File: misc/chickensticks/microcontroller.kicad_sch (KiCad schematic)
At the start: 41 parts, among them J1 Conn_01x05_Pin, J2 HRO_TYPE-C-31-M-12, J3 Conn_01x04, J4 Conn_01x06, J5 Conn_01x06, J6 Conn_01x04, J7 Conn_01x04, Q3 2N7002, SW1 SKRPANE010, SW2 EC11E18244AU, U1 USBLC6-2SC6, U2 STM32L433CCTx, U3 TJA1042T-3, Y1 25 MHz

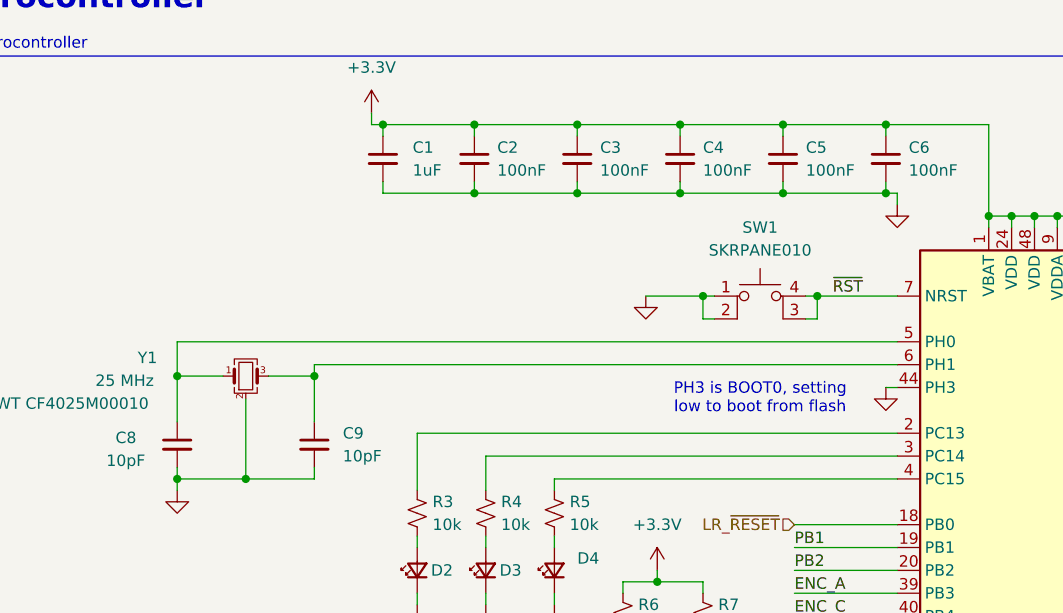
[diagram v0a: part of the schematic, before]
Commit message: the great flatpak and kicad 10.0.6 migration
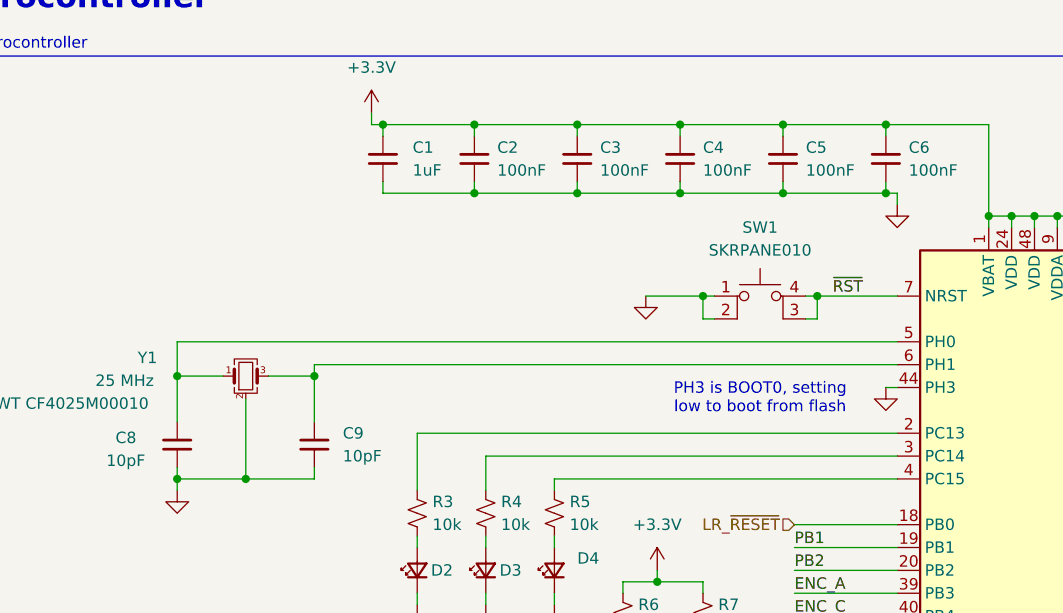
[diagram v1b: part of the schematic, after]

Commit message: Document setup, update template, and use an ampersand when referring to APRL
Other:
- company: Aggie Propulsion and Rocketry Lab -> Aggie Propulsion & Rocketry Lab
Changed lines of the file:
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@@
 		(title "Chickenstick")
 		(rev "0")
-		(company "Aggie Propulsion and Rocketry Lab")
+		(company "Aggie Propulsion & Rocketry Lab")
 		(comment 1 "Drawn by: Nolan Poe")
 		(comment 2 "Reviewed by: Daniel Fan (and hopefully Tim Solberg)")
